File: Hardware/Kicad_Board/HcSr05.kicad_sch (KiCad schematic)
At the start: 9 parts, among them U10 HC-SR04_Ultrasonic_Sensor, U11 HC-SR04_Ultrasonic_Sensor, U7 BOB-12009, U8 HC-SR04_Ultrasonic_Sensor, U9 HC-SR04_Ultrasonic_Sensor

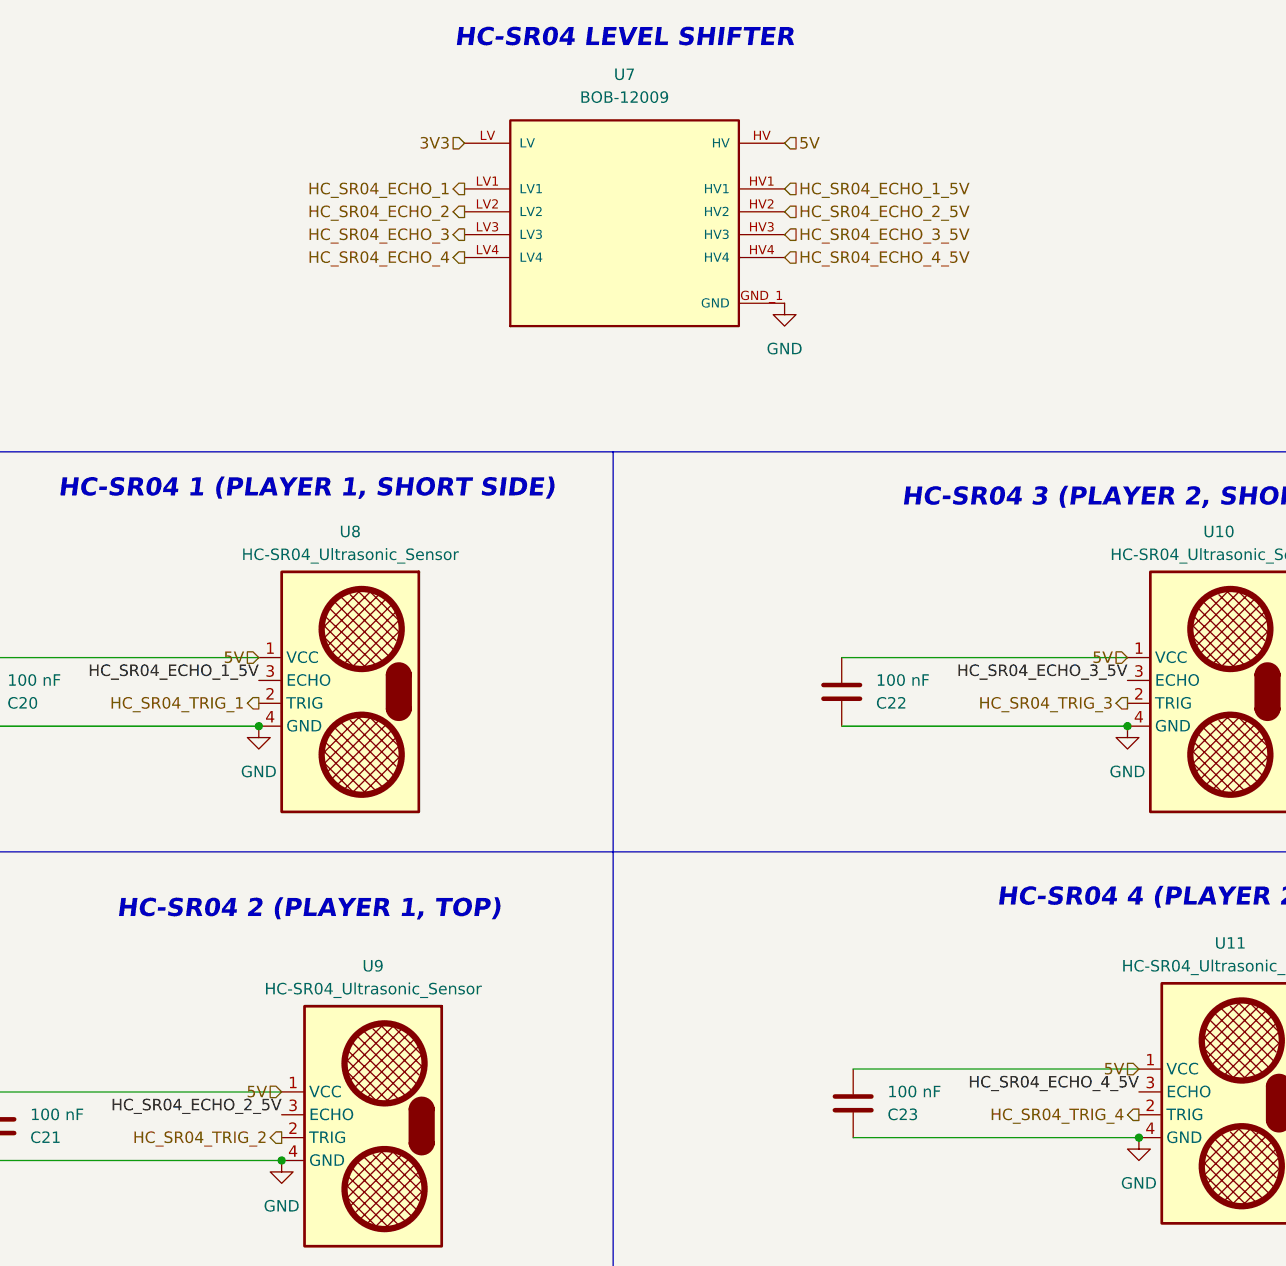
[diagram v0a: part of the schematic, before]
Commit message: Added Kicad proto board
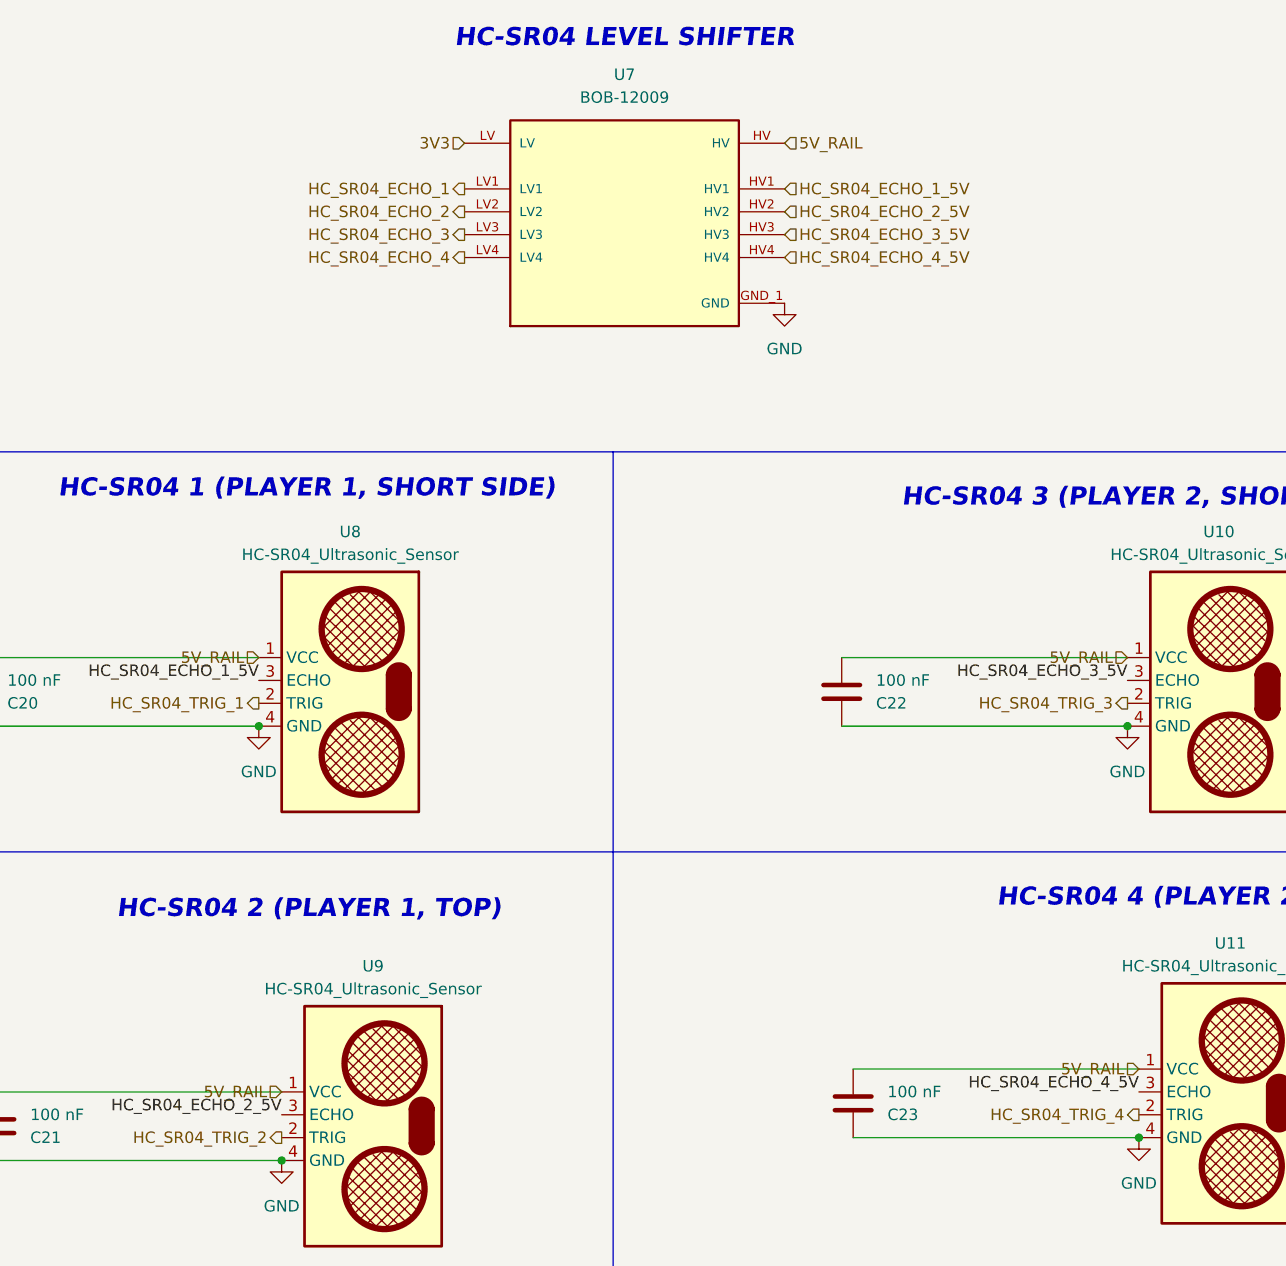
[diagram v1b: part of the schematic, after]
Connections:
- net 5V renamed 5V_RAIL
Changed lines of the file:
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@@
 		)
 	)
-	(hierarchical_label "5V"
+	(hierarchical_label "5V_RAIL"
 		(shape input)
 		(at 154.94 41.91 0)
@@
 		)
 	)
-	(hierarchical_label "5V"
+	(hierarchical_label "5V_RAIL"
 		(shape input)
 		(at 99.06 147.32 180)
@@
 		)
 	)
-	(hierarchical_label "5V"
+	(hierarchical_label "5V_RAIL"
 		(shape input)
 		(at 193.04 99.06 180)
@@
 		)
 	)
-	(hierarchical_label "5V"
+	(hierarchical_label "5V_RAIL"
 		(shape input)
 		(at 96.52 99.06 180)
@@
 		)
 	)
-	(hierarchical_label "5V"
+	(hierarchical_label "5V_RAIL"
 		(shape input)
 		(at 194.31 144.78 180)
@@
 		(exclude_from_sim no)
 		(in_bom yes)
-		(on_board no)
+		(on_board yes)
 		(in_pos_files yes)
 		(dnp no)
@@
 		(exclude_from_sim no)
 		(in_bom yes)
-		(on_board no)
+		(on_board yes)
 		(in_pos_files yes)
 		(dnp no)
@@
 		(exclude_from_sim no)
 		(in_bom yes)
-		(on_board no)
+		(on_board yes)
 		(in_pos_files yes)
 		(dnp no)
@@
 		(exclude_from_sim no)
 		(in_bom yes)
-		(on_board no)
+		(on_board yes)
 		(in_pos_files yes)
 		(dnp no)
@@
 		(exclude_from_sim no)
 		(in_bom yes)
-		(on_board no)
+		(on_board yes)
 		(in_pos_files yes)
 		(dnp no)
@@
 		(exclude_from_sim no)
 		(in_bom yes)
-		(on_board no)
+		(on_board yes)
 		(in_pos_files yes)
 		(dnp no)
@@
 		(exclude_from_sim no)
 		(in_bom yes)
-		(on_board no)
+		(on_board yes)
 		(in_pos_files yes)
 		(dnp no)
@@
 		(exclude_from_sim no)
 		(in_bom yes)
-		(on_board no)
+		(on_board yes)
 		(in_pos_files yes)
 		(dnp no)
